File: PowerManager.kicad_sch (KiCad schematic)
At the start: 13 parts, among them U2 LM317_SOT-223

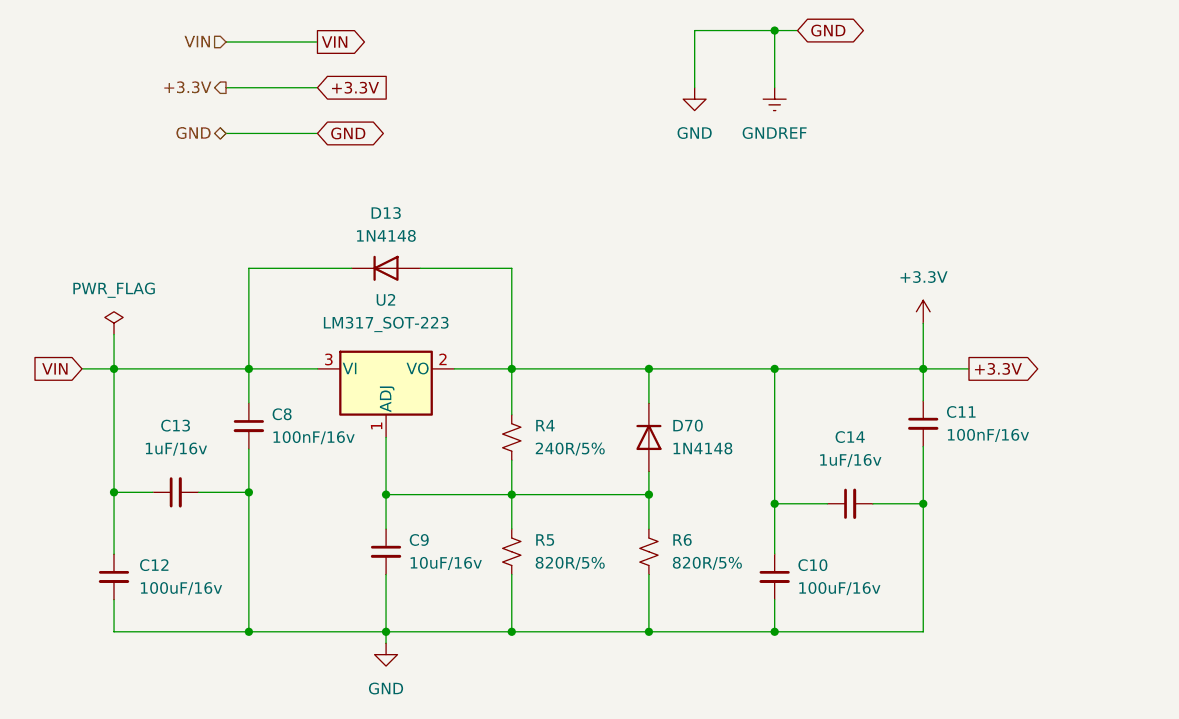
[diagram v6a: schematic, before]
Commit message: change LDO ic and PCB layout
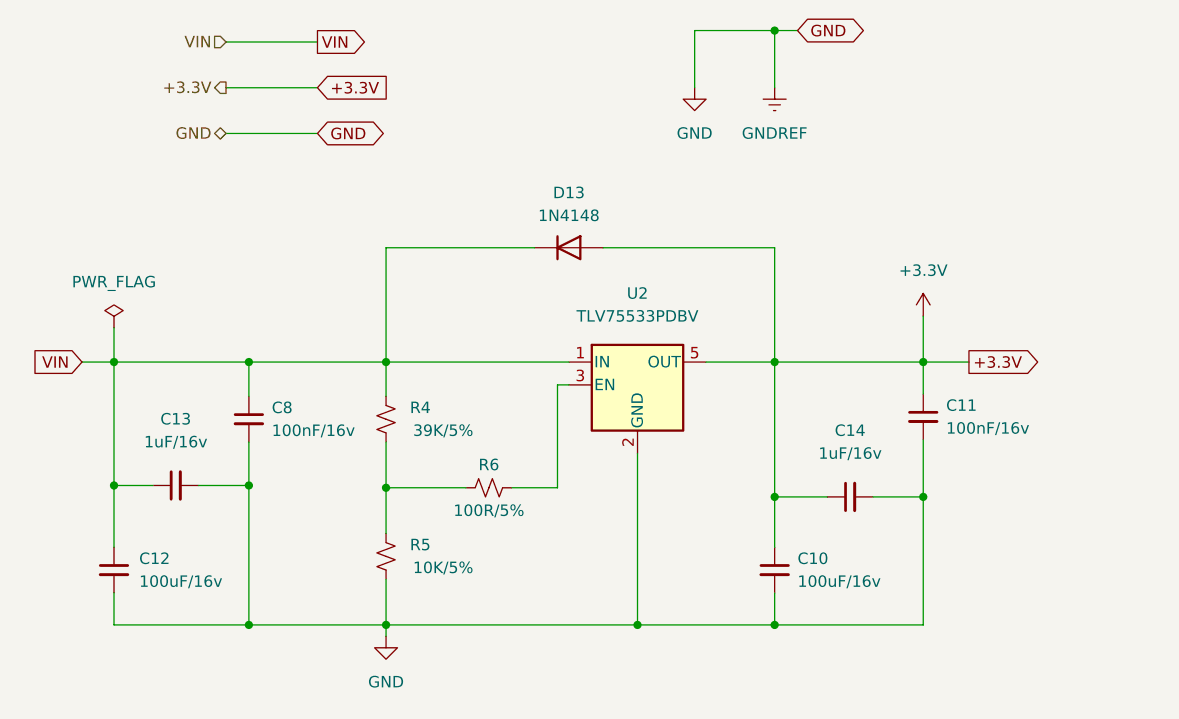
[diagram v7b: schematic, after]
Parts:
- removed C9: 10uF/16v, Capacitor_SMD:C_0805_2012Metric, symbol Device:C_Small
- removed D70: 1N4148, Diode_SMD:D_0805_2012Metric, symbol Diode:1SS355VM
- removed U2: LM317_SOT-223, Package_TO_SOT_SMD:SOT-223-3_TabPin2, symbol Regulator_Linear:LM317_SOT-223
- added U2: TLV75533PDBV, Package_TO_SOT_SMD:SOT-23-5, symbol Regulator_Linear:TLV75533PDBV
- R4: value 240R/5% -> 39K/5%
- R5: value 820R/5% -> 10K/5%
- R6: value 820R/5% -> 100R/5%
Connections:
- net +3.3V: now also U2.5 (OUT); no longer R4.1
- net GND: now also U2.2 (GND); no longer R6.2
- net VIN: now also R4.2, U2.1 (IN)
- new net: R4.1, R5.1, R6.2
- new net: R6.1, U2.3 (EN)
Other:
- moved on the sheet: C10, C11, C12, C13, C14, C8, D13

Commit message: modify power manager value
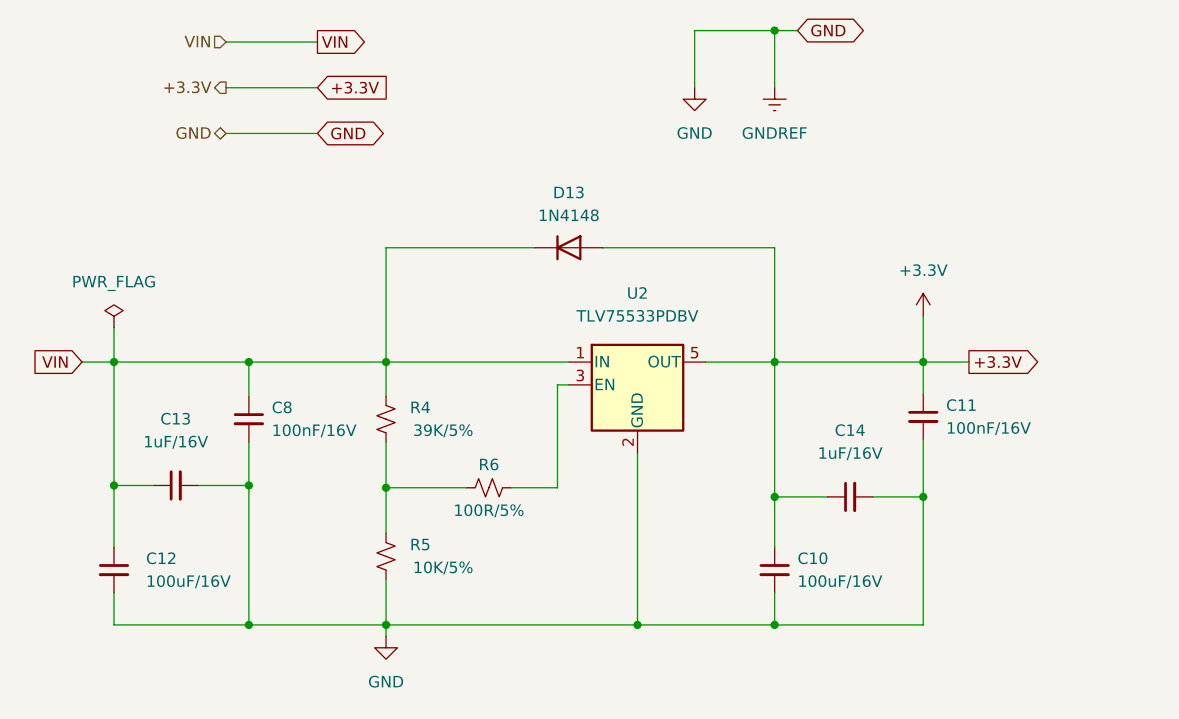
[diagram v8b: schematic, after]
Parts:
- C10, C12: value 100uF/16v -> 100uF/16V
- C11, C8: value 100nF/16v -> 100nF/16V
- C13, C14: value 1uF/16v -> 1uF/16V
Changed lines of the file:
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@@
     (in_bom yes) (on_board yes) (fields_autoplaced)
     (property "Reference" "C13" (id 0) (at 109.9883 115.57 90))
-    (property "Value" "1uF/16v" (id 1) (at 109.9883 118.11 90))
+    (property "Value" "1uF/16V" (id 1) (at 109.9883 118.11 90))
     (property "Footprint" "Capacitor_SMD:C_0603_1608Metric" (id 2) (at 109.982 122.936 0)
       (effects (font (size 1.27 1.27)) hide)
@@
       (effects (font (size 1.27 1.27)) (justify left))
     )
-    (property "Value" "100nF/16v" (id 1) (at 120.65 116.8462 0)
+    (property "Value" "100nF/16V" (id 1) (at 120.65 116.8462 0)
       (effects (font (size 1.27 1.27)) (justify left))
     )
@@
   (symbol (lib_id "Device:C_Small") (at 103.124 132.334 0) (unit 1)
     (in_bom yes) (on_board yes) (fields_autoplaced)
-    (property "Reference" "C12" (id 0) (at 105.918 131.0702 0)
+    (property "Reference" "C12" (id 0) (at 106.68 131.0702 0)
       (effects (font (size 1.27 1.27)) (justify left))
     )
-    (property "Value" "100uF/16v" (id 1) (at 105.918 133.6102 0)
+    (property "Value" "100uF/16V" (id 1) (at 106.68 133.6102 0)
       (effects (font (size 1.27 1.27)) (justify left))
     )
@@
       (effects (font (size 1.27 1.27)) (justify left))
     )
-    (property "Value" "100nF/16v" (id 1) (at 195.58 116.5922 0)
+    (property "Value" "100nF/16V" (id 1) (at 195.58 116.5922 0)
       (effects (font (size 1.27 1.27)) (justify left))
     )
@@
     (in_bom yes) (on_board yes) (fields_autoplaced)
     (property "Reference" "C14" (id 0) (at 184.9183 116.84 90))
-    (property "Value" "1uF/16v" (id 1) (at 184.9183 119.38 90))
+    (property "Value" "1uF/16V" (id 1) (at 184.9183 119.38 90))
     (property "Footprint" "Capacitor_SMD:C_0603_1608Metric" (id 2) (at 184.912 124.206 0)
       (effects (font (size 1.27 1.27)) hide)
@@
       (effects (font (size 1.27 1.27)) (justify left))
     )
-    (property "Value" "100uF/16v" (id 1) (at 179.07 133.6102 0)
+    (property "Value" "100uF/16V" (id 1) (at 179.07 133.6102 0)
       (effects (font (size 1.27 1.27)) (justify left))
     )
